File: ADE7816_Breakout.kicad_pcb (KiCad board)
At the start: 2 copper layers, 66 x 76.2 mm, 56 parts, among them J1 AudioJack3, J2 AudioJack3, J3 AudioJack3, J4 AudioJack3, J5 AudioJack3, J6 AudioJack3, J7 Barrel_Jack_Switch, J8 Conn_01x10, U1 ADE7816ACPZ, Y1 16.384MHz

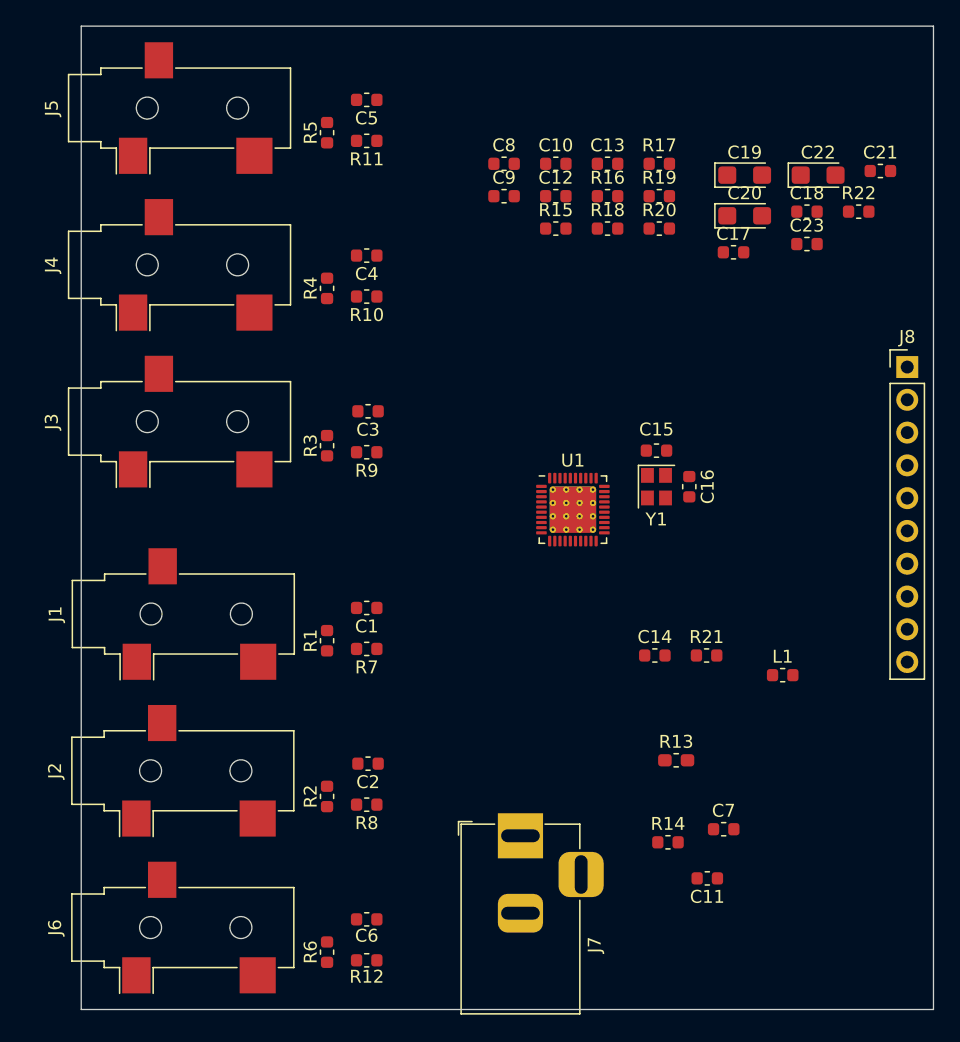
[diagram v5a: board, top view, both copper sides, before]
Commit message: make ridiculously thin traces for route attempt
Signed-off-by: Tisham Dhar <whatnickd@gmail.com>
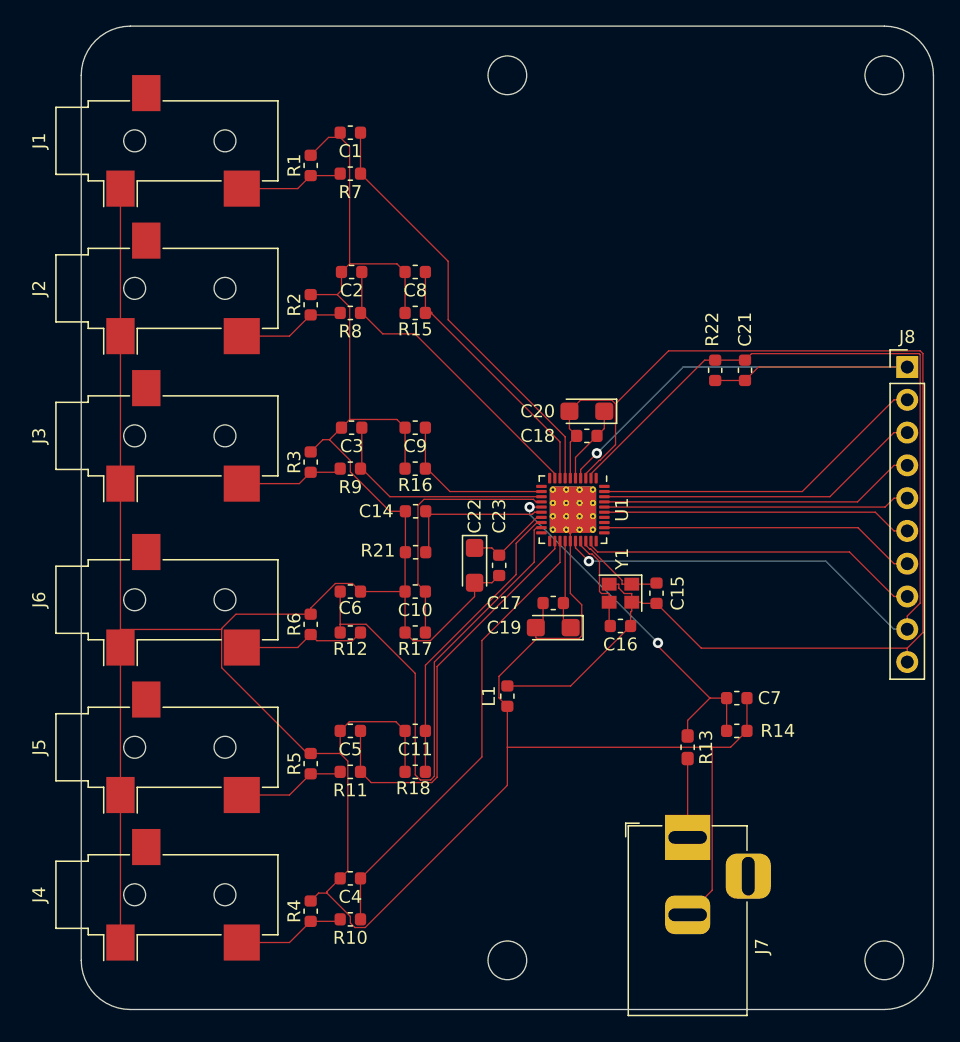
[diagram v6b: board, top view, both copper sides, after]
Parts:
- removed C12, C13: 22n, Capacitor_SMD:C_0603_1608Metric
- removed R19, R20: 1k, Resistor_SMD:R_0603_1608Metric
- added H1: MountingHole, MountingHole:MountingHole_3mm, F.Cu at (127.0, 34.3)
- added H2: MountingHole, MountingHole:MountingHole_3mm, F.Cu at (127.0, 102.9)
- added H3: MountingHole, MountingHole:MountingHole_3mm, F.Cu at (156.2, 34.3)
- added H4: MountingHole, MountingHole:MountingHole_3mm, F.Cu at (156.2, 102.9)
- moved J5 49.5 mm to (100.6, 86.4)
- moved R5 48.9 mm to (111.8, 87.6)
- moved C5 48.9 mm to (114.8, 85.1)
- moved R11 48.9 mm to (114.8, 88.3)
- moved J4 48.8 mm to (100.6, 97.8)
- moved R4 48.3 mm to (111.8, 99.1)
- moved C4 48.3 mm to (114.8, 96.5)
- moved R10 48.3 mm to (114.8, 99.7)
- moved R18 44.7 mm to (119.9, 88.3)
- moved R17 41.0 mm to (119.9, 77.5)
- moved C22 40.3 mm to (124.5, 72.3), turned to 270 degrees
- moved R2 38.1 mm to (111.8, 52.1)
- moved C2 38.1 mm to (114.9, 49.5)
- moved R8 38.1 mm to (114.8, 52.7)
- moved C19 38.1 mm to (130.6, 77.1), turned to 180 degrees
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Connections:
- net Net-(C15-Pad2) renamed /meter_module/CLKOUT
- J8 pad 2: /meter_module/HSCLK -> /meter_module/~CS
- J8 pad 3: /meter_module/SCLK -> /meter_module/MOSI
- J8 pad 4: /meter_module/MOSI -> /meter_module/MISO
- J8 pad 5: /meter_module/MISO -> /meter_module/SCLK
- J8 pad 6: /meter_module/~CS -> /meter_module/HSCLK
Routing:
- net GNDA: track 0.00 -> 296.7 mm
- net GNDD: track 0.00 -> 105.5 mm
- net +3V3: track 0.00 -> 80.3 mm, vias 0 -> 1
- net /meter_module/~RESET: track 0.00 -> 44.6 mm, vias 0 -> 1
- net IFP: track 0.00 -> 43.1 mm
- net IDP: track 0.00 -> 35.7 mm
- net IAP: track 0.00 -> 33.3 mm
- net IEP: track 0.00 -> 31.7 mm
- net VP: track 0.00 -> 29.0 mm, vias 0 -> 2
- net /meter_module/~IRQ0: track 0.00 -> 26.5 mm
- net /meter_module/~CS: track 0.00 -> 26.4 mm
- net /meter_module/MOSI: track 0.00 -> 25.5 mm
- net /meter_module/MISO: track 0.00 -> 24.6 mm
- net /meter_module/~IRQ1: track 0.00 -> 24.6 mm
- net /meter_module/HSCLK: track 0.00 -> 24.1 mm
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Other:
- outline, holes or cut-outs redrawn

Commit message: Some routing
Signed-off-by: Tisham Dhar <whatnickd@gmail.com>
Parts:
- turned C6 to 180 degrees
- turned R12 to 180 degrees
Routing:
- net GNDA: track 296.7 -> 136.0 mm, vias 0 -> 5
- net GNDD: track 105.5 -> 0.00 mm
- net +3V3: track 80.3 -> 0.00 mm, vias 1 -> 0
- net /meter_module/~RESET: track 44.6 -> 0.00 mm, vias 1 -> 0
- net IFP: track 43.1 -> 0.00 mm
- net IDP: track 35.7 -> 0.00 mm
- net IAP: track 33.3 -> 0.00 mm
- net IEP: track 31.7 -> 0.00 mm
- net VP: track 29.0 -> 0.00 mm, vias 2 -> 0
- net /meter_module/~IRQ0: track 26.5 -> 0.00 mm
- net /meter_module/~CS: track 26.4 -> 0.00 mm
- net /meter_module/MOSI: track 25.5 -> 0.00 mm
- net /meter_module/MISO: track 24.6 -> 0.00 mm
- net /meter_module/~IRQ1: track 24.6 -> 0.00 mm
- net /meter_module/HSCLK: track 24.1 -> 0.00 mm
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
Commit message: Violate DRC and get some routing done
Signed-off-by: Tisham Dhar <whatnickd@gmail.com>
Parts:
- moved L1 6.76 mm to (133.7, 81.5), turned to 0 degrees
- moved C14 6.33 mm to (120.0, 74.4)
- moved R21 6.33 mm to (120.0, 77.6)
- moved C10 5.94 mm to (119.9, 68.4)
- moved R17 5.94 mm to (119.9, 71.5)
- moved C17 1.05 mm to (131.6, 75.4), turned to 0 degrees
- moved C19 1.05 mm to (131.6, 77.3), turned to 0 degrees
- turned C21 to 90 degrees
- turned R22 to 90 degrees
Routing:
- net GNDA: track 136.0 -> 224.2 mm, vias 5 -> 13
- net +3V3: track 0.00 -> 46.2 mm, vias 0 -> 2
- net GNDD: track 0.00 -> 38.6 mm
- net IDP: track 0.00 -> 37.3 mm
- net IEP: track 0.00 -> 35.5 mm
- net IAP: track 0.00 -> 34.8 mm
- net /meter_module/~RESET: track 0.00 -> 30.1 mm
- net /meter_module/~IRQ0: track 0.00 -> 27.0 mm
- net /meter_module/~CS: track 0.00 -> 26.4 mm
- net /meter_module/MOSI: track 0.00 -> 25.5 mm
- net IFP: track 0.00 -> 25.5 mm
- net IN: track 0.00 -> 24.8 mm, vias 0 -> 2
- net /meter_module/MISO: track 0.00 -> 24.6 mm
- net /meter_module/~IRQ1: track 0.00 -> 24.6 mm
- net /meter_module/HSCLK: track 0.00 -> 24.1 mm
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- added copper zone on B.Cu, net GNDA
- added copper zone on F.Cu, net GNDA
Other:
- rule trace_min: 0.2 -> 0.15
